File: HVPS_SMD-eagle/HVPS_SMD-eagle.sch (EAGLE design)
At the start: 17 parts, among them Q1 DMT10H010LK3, T1 749196141, U1 LM3478MM/NOPB

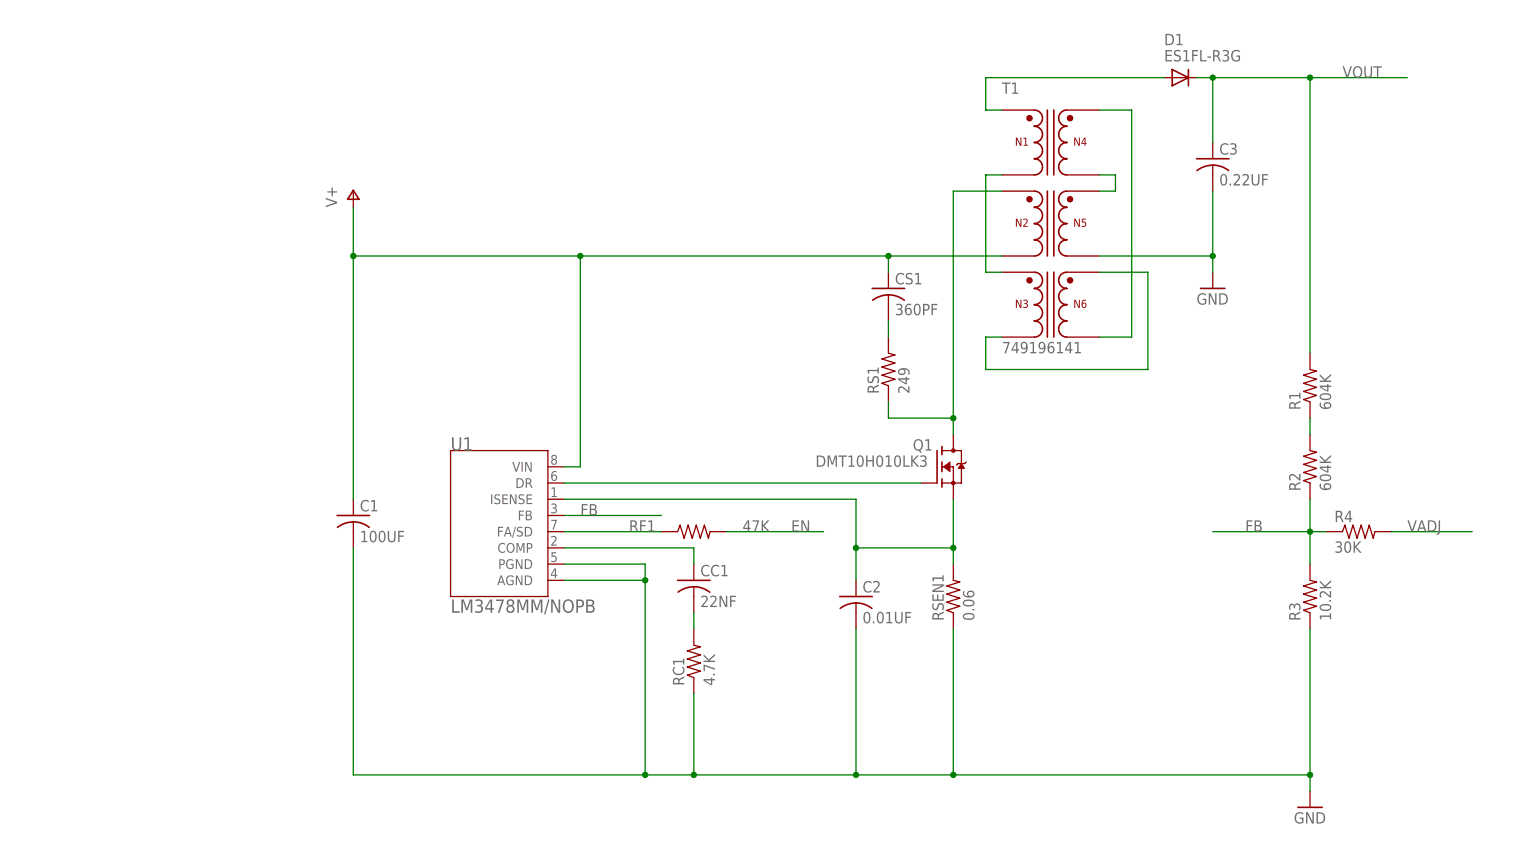
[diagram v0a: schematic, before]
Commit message: -Completed layout. -Added headers.
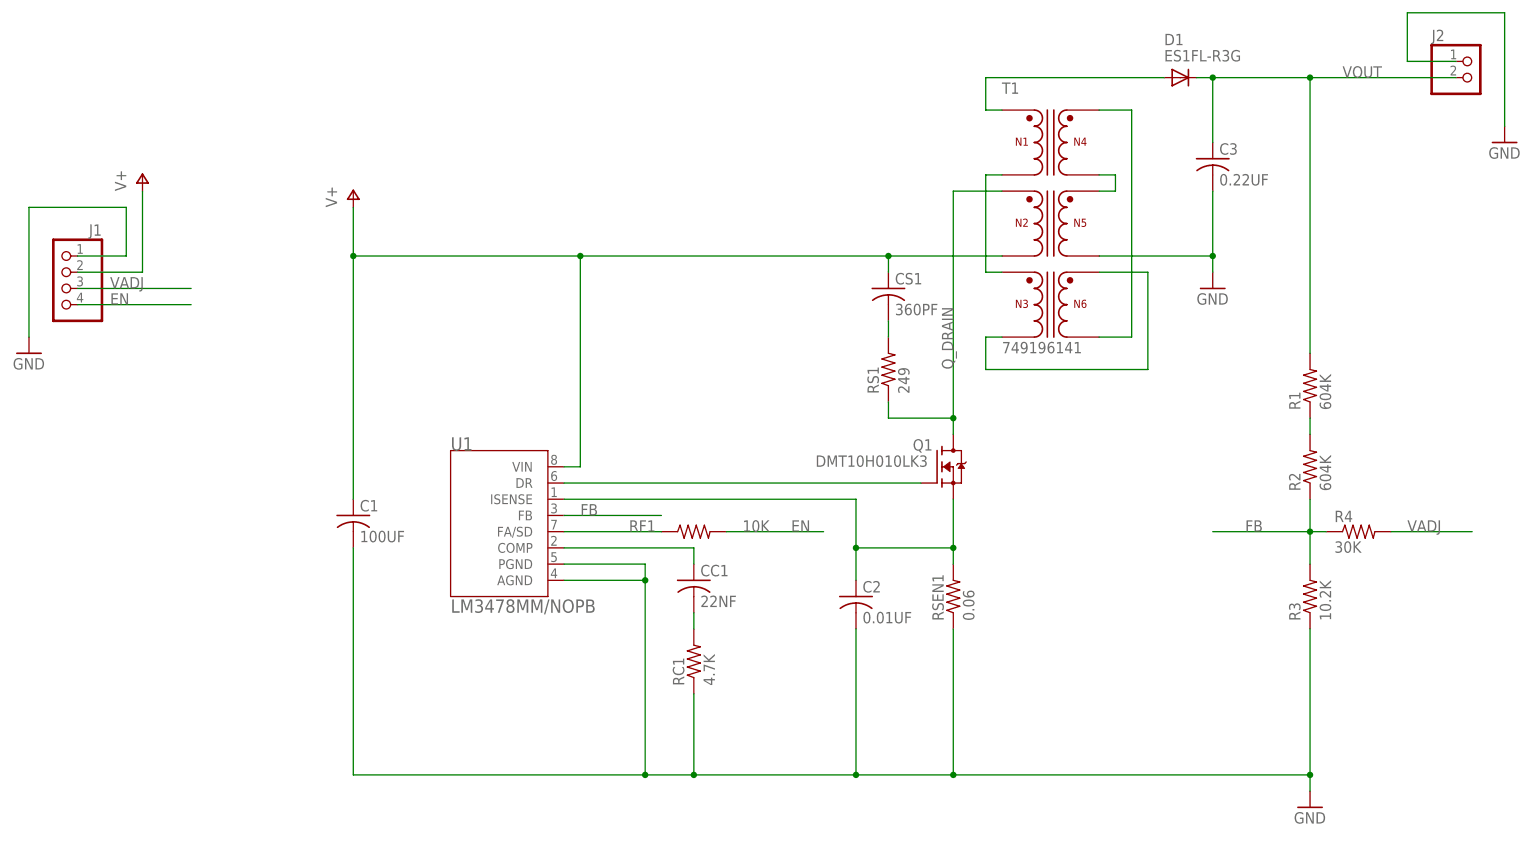
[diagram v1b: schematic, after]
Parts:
- added J1: (no value), pinhead:PINHD-1X4
- added J2: (no value), pinhead:PINHD-1X2
- RF1: value 47K -> 10K; device rcl:R-US_R0805 -> rcl:R-US_R0603
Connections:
- net N$5 renamed Q_DRAIN
- net EN: now also J1.4
- net GND: now also J1.1, J2.1
- net V+: now also J1.2
- net VADJ: now also J1.3
- net VOUT: now also J2.2

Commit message: -Updated design rules. -Added proper FA/SD signal path.
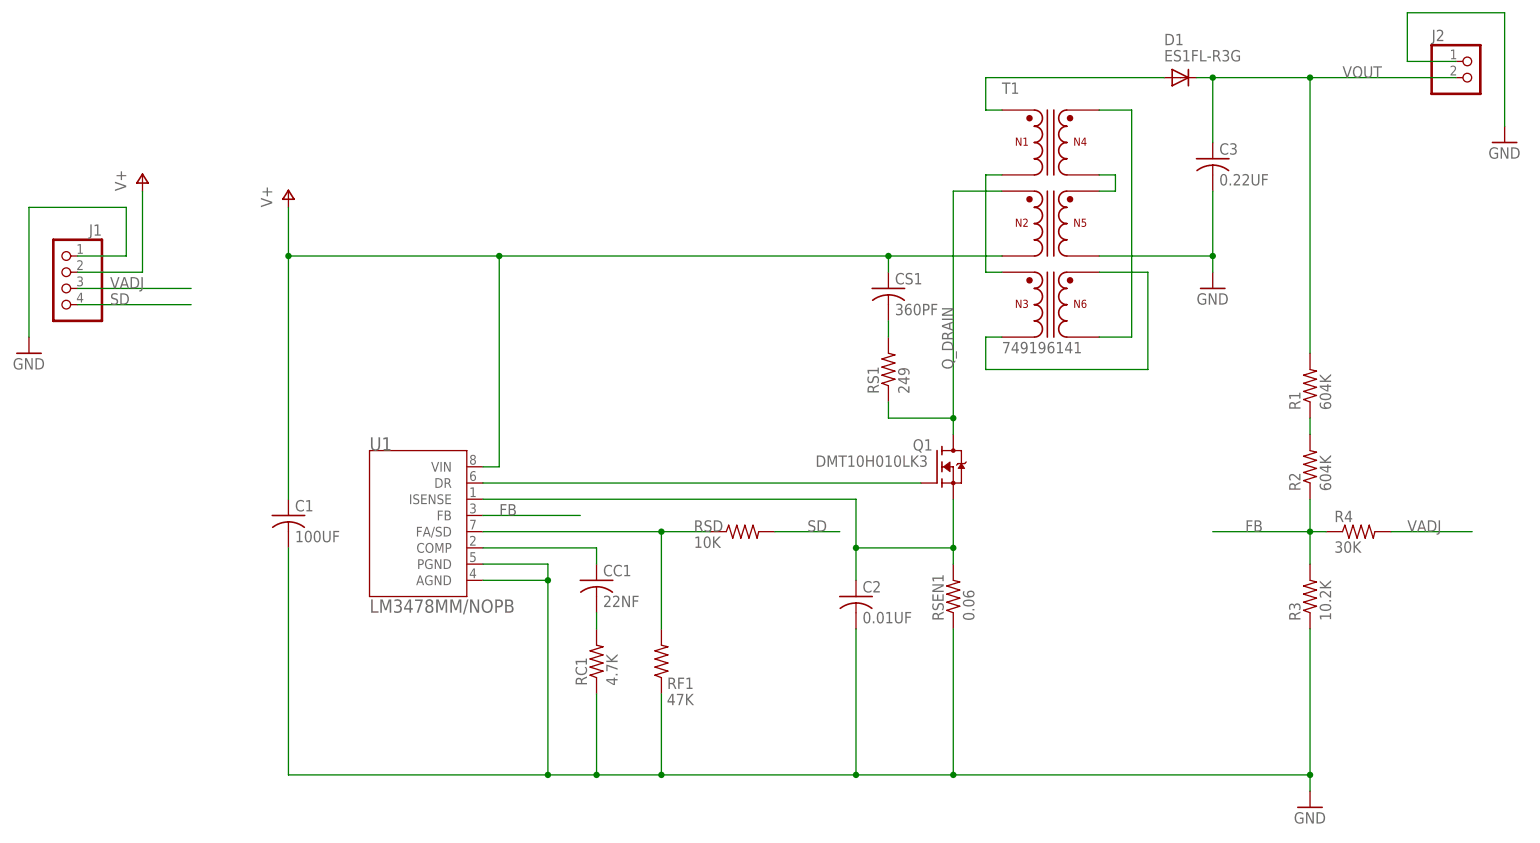
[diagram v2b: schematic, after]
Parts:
- added RSD: 10K, rcl:R-US_R0603
- RF1: value 10K -> 47K
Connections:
- removed net EN: J1.4, RF1.2
- new net SD: J1.4, RSD.2
- net GND: now also RF1.1
- net N$1: now also RF1.2, RSD.1; no longer RF1.1
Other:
- moved on the sheet: C1, CC1, RC1, RF1, U1
